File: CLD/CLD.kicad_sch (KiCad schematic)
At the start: 30 parts, among them J1 Conn_01x02, J2 Conn_01x02, J3 Conn_01x02, J4 Conn_01x02, J5 Conn_02x05_Counter_Clockwise, Q1 BSC072N08NS5, U1 STM32F103TBUx, U2 FAN3111E, U3 INA180A1, U4 MCP2551-I-SN

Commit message: update 17/09
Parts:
- removed R2: 50r, symbol Device:R
- removed U1: STM32F103TBUx, Package_DFN_QFN:QFN-36-1EP_6x6mm_P0.5mm_EP4.1x4.1mm, symbol MCU_ST_STM32F1:STM32F103TBUx
- added L1: 0.5uH, Inductor_SMD:L_Bourns-SRN8040_8x8.15mm, symbol Device:L
- added U1: STM32F103CBUx, Package_DFN_QFN:QFN-48-1EP_7x7mm_P0.5mm_EP5.6x5.6mm, symbol MCU_ST_STM32F1:STM32F103CBUx
- C1, C10, C11, C12, C2, C3, C4, C5, C6, C7, C8, C9: footprint (none) -> Capacitor_SMD:C_0201_0603Metric
- D1, D2: footprint (none) -> Diode_SMD:D_0201_0603Metric
- J1, J2, J3, J4: footprint (none) -> Connector_PinHeader_2.54mm:PinHeader_1x02_P2.54mm_Vertical
- J5: footprint (none) -> Connector_PinHeader_1.27mm:PinHeader_2x05_P1.27mm_Vertical_SMD
- R1: footprint (none) -> Resistor_SMD:R_Shunt_Vishay_WSK2512_6332Metric_T1.19mm
- R3, R4, R5, R6: footprint (none) -> Resistor_SMD:R_0201_0603Metric
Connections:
- net +3.3V: now also J5.5 (Pin_5), U1.24 (VDD), U1.36 (VDD), U1.48 (VDD), U1.9 (VDDA)
- net Can_Rx: now also U1.45 (PB8)
- net Can_Tx: now also U1.46 (PB9)
- net Current: now also U1.10 (PA0)
- net GND: now also J5.1 (Pin_1), J5.3 (Pin_3), J5.4 (Pin_4), U1.23 (VSS), U1.35 (VSS), U1.47 (VSS), U1.49 (VSS), U1.8 (VSSA)
- net JTAG_CLK: now also J5.7 (Pin_7), U1.37 (PA14)
- net JTAG_D0: now also J5.8 (Pin_8), U1.39 (PB3)
- net JTAG_D1: now also J5.9 (Pin_9), U1.38 (PA15)
- net JTAG_RST: now also J5.10 (Pin_10), U1.40 (PB4)
- net JTAG_SWDIO: now also J5.6 (Pin_6), U1.34 (PA13)
- net Mos_EN: now also U1.15 (PA5)
- net at Q1.1 (S), Q1.2 (S), Q1.3 (S): now also L1.1
- net at R1.1, U3.3 (+): now also L1.2
- net at D2.1 (K): now also U1.13 (PA3)
- net at D1.1 (K): now also U1.14 (PA4)
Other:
- moved on the sheet: C1, C10, C11, C12, C2, C3, C4, C5, C6, C7, C8, C9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

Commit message: PCB
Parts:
- removed C10, C11, C2, C3, C4: 100n, Capacitor_SMD:C_0201_0603Metric, symbol Device:C
- removed C12, C5: 1u, Capacitor_SMD:C_0201_0603Metric, symbol Device:C
- added C13: 100n, Capacitor_SMD:C_0603_1608Metric, symbol Device:C
- added R2, R7: 10, Resistor_SMD:R_0603_1608Metric, symbol Device:R
- C1, C6, C7, C8, C9: footprint Capacitor_SMD:C_0201_0603Metric -> Capacitor_SMD:C_0603_1608Metric
- D1, D2: footprint Diode_SMD:D_0201_0603Metric -> Diode_SMD:D_0603_1608Metric
- R1: value 0.5mOhm -> 22mOhm; footprint Resistor_SMD:R_Shunt_Vishay_WSK2512_6332Metric_T1.19mm -> Resistor_SMD:R_1206_3216Metric
- R3, R4, R5, R6: footprint Resistor_SMD:R_0201_0603Metric -> Resistor_SMD:R_0603_1608Metric
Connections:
- net GND: now also R7.1; no longer U3.4 (-)
- net at R3.1: now also D1.1 (K); no longer D1.2 (A)
- net at L1.2, R1.1: now also R2.1; no longer U3.3 (+)
- net at D2.1 (K): now also R4.1; no longer U1.13 (PA3)
- net at D2.2 (A): now also U1.13 (PA3); no longer R4.1
- net at U1.14 (PA4): now also D1.2 (A); no longer D1.1 (K)
- new net: C13.1, R2.2, U3.3 (+)
- new net: C13.2, R7.2, U3.4 (-)
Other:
- note removed: "Cap Vin > 25V"
- moved on the sheet: C1, C6, C7, C8, C9, D1, D2, J1, L1, Q1, R1, U2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

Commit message: howdy
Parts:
- added C2, C3: 100n, Capacitor_SMD:C_0603_1608Metric, symbol Device:C
- added D3: LED, Diode_SMD:D_0603_1608Metric, symbol Device:LED
- added R8: 50r, Resistor_SMD:R_0603_1608Metric, symbol Device:R
- added U5: AP2112K-3.3, Package_TO_SOT_SMD:SOT-23-5, symbol Regulator_Linear:AP2112K-3.3
- R3, R4: value R -> 50r
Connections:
- net +3.3V: now also C3.1, U5.5 (VOUT)
- net +5V: now also C2.1, U5.1 (VIN), U5.3 (EN)
- net GND: now also D1.1 (K), D2.1 (K), C2.2, C3.2, D3.1 (K), U5.2 (GND); no longer R3.2, R4.2
- net at R3.1: now also U1.14 (PA4); no longer D1.1 (K)
- net at R4.1: now also U1.13 (PA3); no longer D2.1 (K)
- net at D2.2 (A): now also R4.2; no longer U1.13 (PA3)
- net at D1.2 (A): now also R3.2; no longer U1.14 (PA4)
- net at U1.26 (PB13): now also R8.1
- new net: D3.2 (A), R8.2
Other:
- moved on the sheet: D1, D2

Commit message: PCB routed
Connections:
- net Mos_EN: now also U1.21 (PB10); no longer U1.15 (PA5)
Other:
- company: (none) -> Jack Baker
- title: (none) -> Smart Load Switch
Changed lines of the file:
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@@
 	(generator_version "8.0")
 	(paper "A4")
+	(title_block
+		(title "Smart Load Switch")
+		(date "2024-05-20")
+		(rev "V1.0")
+		(company "Jack Baker")
+	)
 	(junction
 		(at 234.95 31.75)
@@
 		(pts
 			(xy 21.59 31.75) (xy 34.29 31.75)
+		)
+		(stroke
+			(width 0)
+			(type default)
+		)
+	)
+	(wire
+		(pts
+			(xy 24.13 142.24) (xy 33.02 142.24)
 		)
 		(stroke
@@
 		)
 	)
-	(label "Mos_EN"
-		(at 66.04 101.6 0)
-		(fields_autoplaced yes)
-		(effects
-			(font
-				(size 1.27 1.27)
-			)
-			(justify left bottom)
-		)
-	)
 	(label "JTAG_RST"
 		(at 21.59 127 0)
@@
 		(fields_autoplaced yes)
 		(effects
+			(font
+				(size 1.27 1.27)
+			)
+			(justify left bottom)
+		)
+	)
+	(label "Mos_EN"
+		(at 24.13 142.24 0)
+		(fields_autoplaced yes)
+		(effects

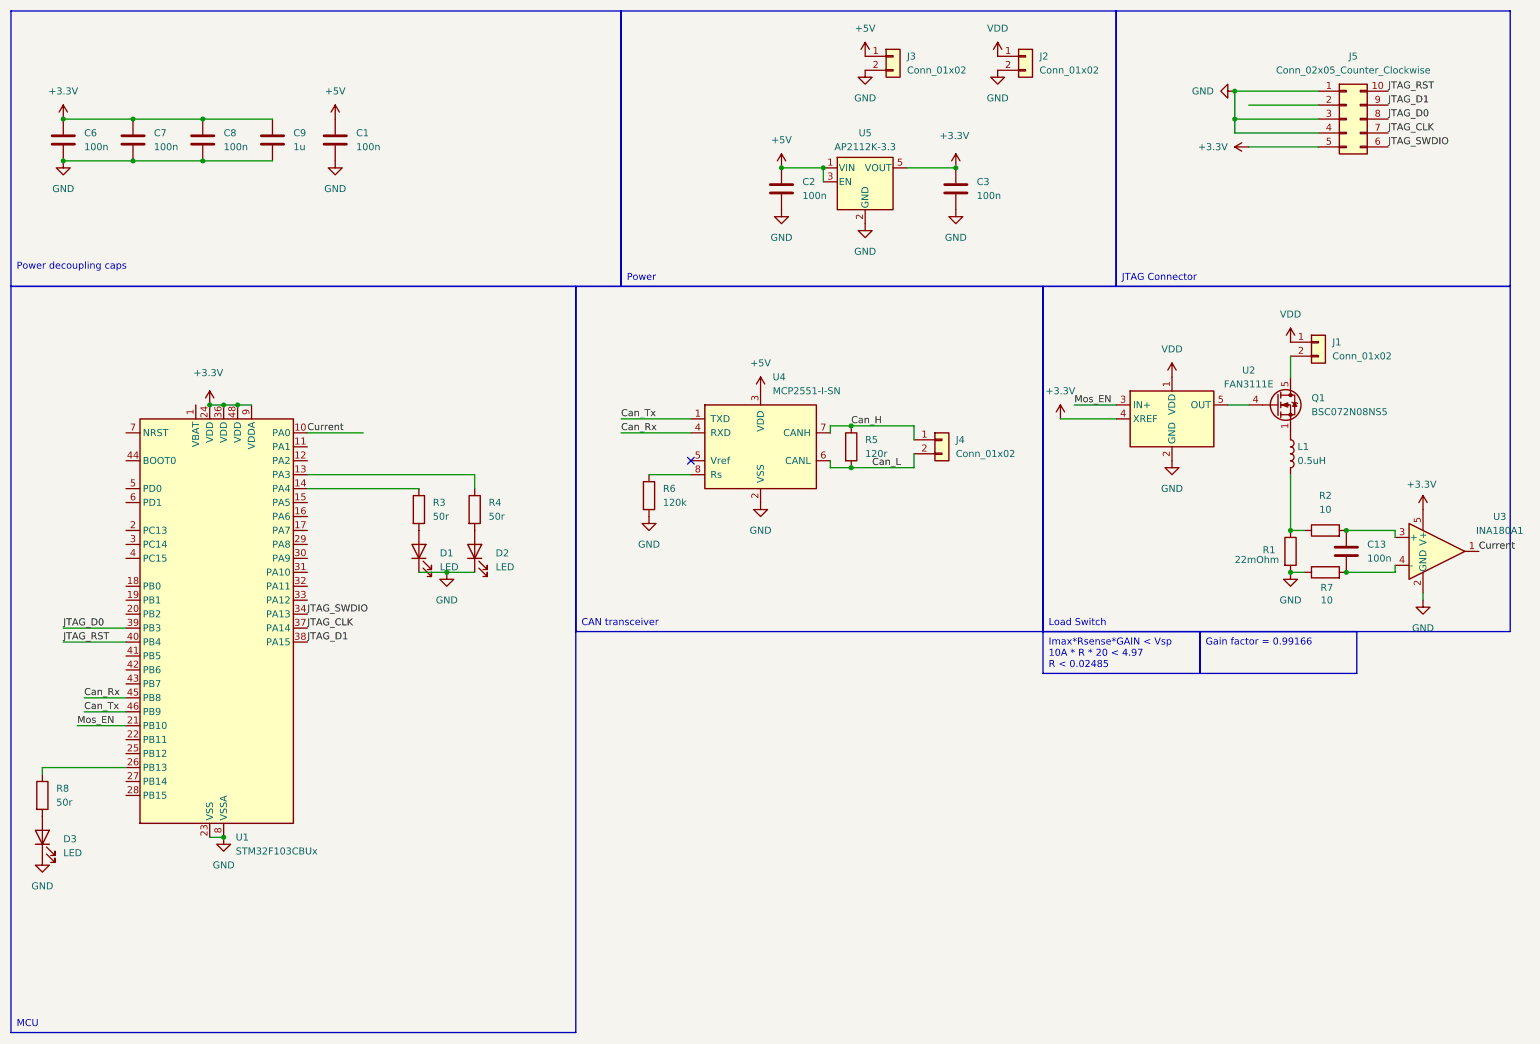
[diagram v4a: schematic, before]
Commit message: add USB + crystal
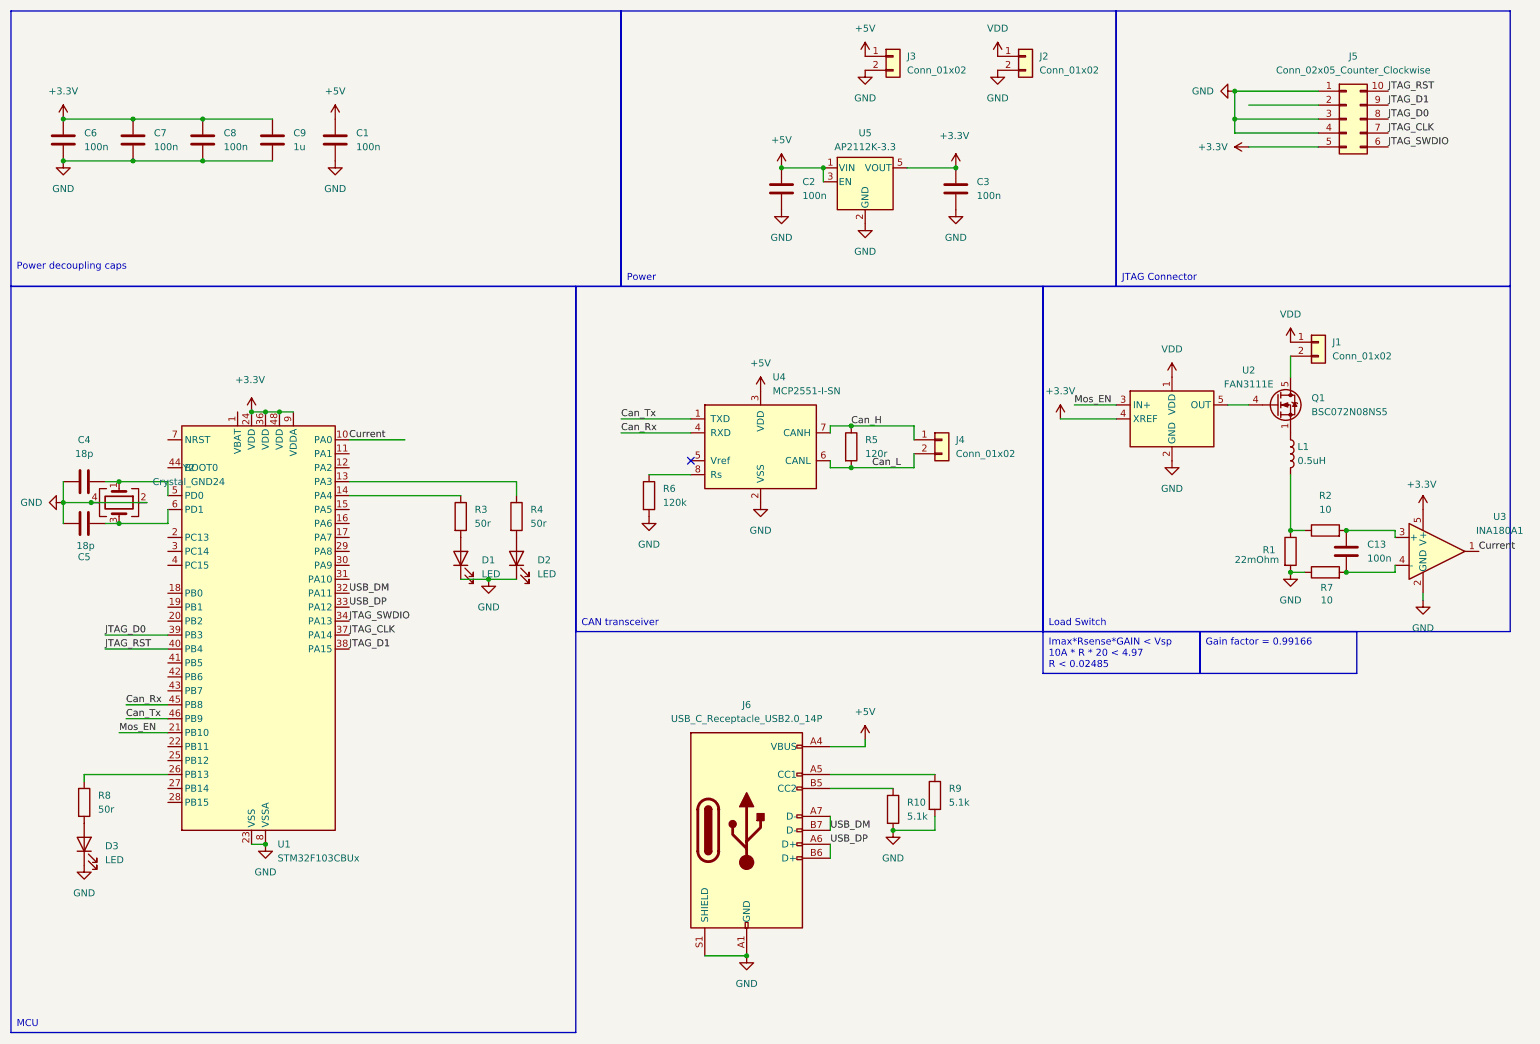
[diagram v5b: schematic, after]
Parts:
- added C4, C5: 18p, Capacitor_SMD:C_0603_1608Metric, symbol Device:C
- added J6: USB_C_Receptacle_USB2.0_14P, Connector_USB:USB_C_Receptacle_GCT_USB4105-xx-A_16P_TopMnt_Horizontal, symbol Connector:USB_C_Receptacle_USB2.0_14P
- added R10, R9: 5.1k, Resistor_SMD:R_0603_1608Metric, symbol Device:R
- added Y2: Crystal_GND24, Crystal:Crystal_SMD_Abracon_ABM3C-4Pin_5.0x3.2mm, symbol Device:Crystal_GND24
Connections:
- net +5V: now also J6.A4 (VBUS), J6.A9 (VBUS), J6.B4 (VBUS), J6.B9 (VBUS)
- net GND: now also C4.1, C5.1, J6.A1 (GND), J6.A12 (GND), J6.B1 (GND), J6.B12 (GND), J6.S1 (SHIELD), R10.2, R9.2, Y2.2, Y2.4
- net USB_DM: now reaches U1.32 (PA11)
- net USB_DM: now also J6.A7 (D-), J6.B7 (D-)
- net USB_DP: now reaches U1.33 (PA12)
- net USB_DP: now also J6.A6 (D+), J6.B6 (D+)
- net at U1.5 (PD0): now also C4.2, Y2.1
- net at U1.6 (PD1): now also C5.2, Y2.3
- new net: J6.A5 (CC1), R9.1
- new net: J6.B5 (CC2), R10.1
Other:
- moved on the sheet: D1, D2, D3, R3, R4, R8, U1

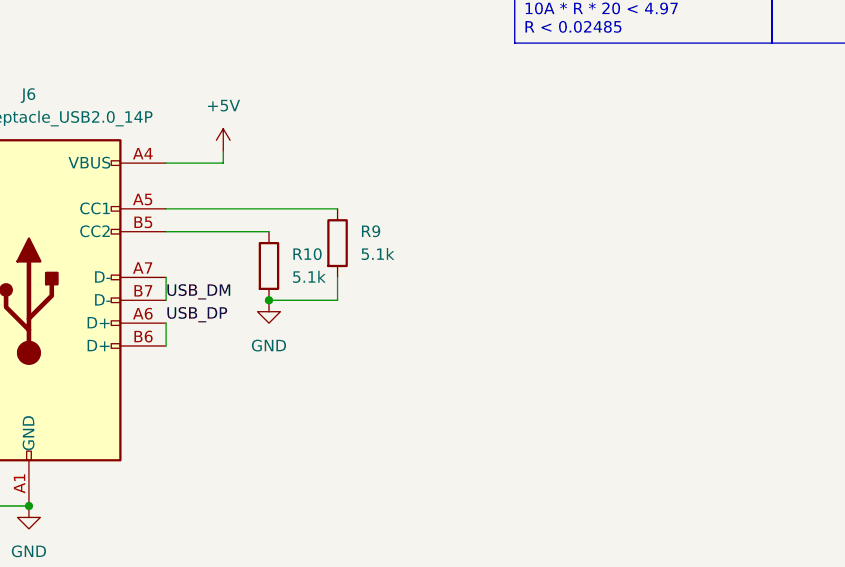
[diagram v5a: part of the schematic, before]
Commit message: added USB serial resistors oops
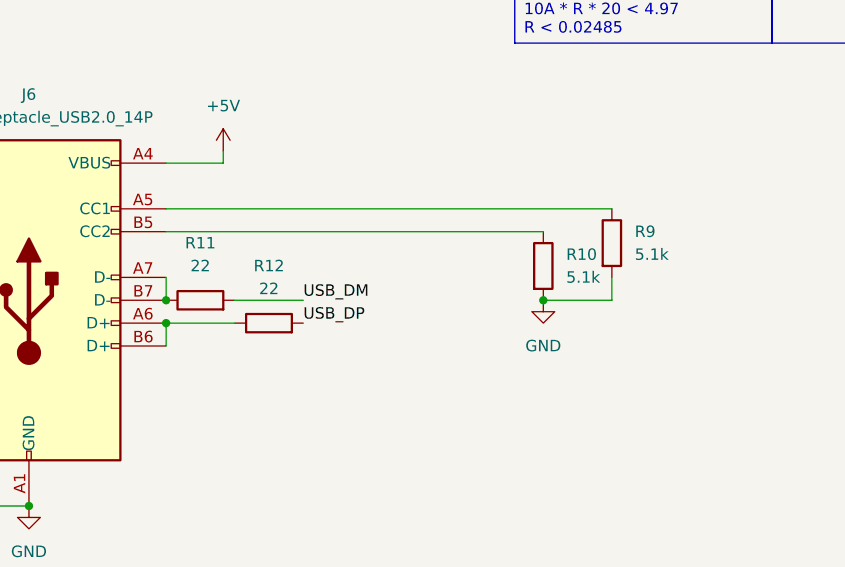
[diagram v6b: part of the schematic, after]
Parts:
- added R11, R12: 22, Resistor_SMD:R_0603_1608Metric, symbol Device:R
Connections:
- net USB_DM: now also R11.2; no longer J6.A7 (D-), J6.B7 (D-)
- net USB_DP: now also R12.2; no longer J6.A6 (D+), J6.B6 (D+)
- new net: J6.A6 (D+), J6.B6 (D+), R12.1
- new net: J6.A7 (D-), J6.B7 (D-), R11.1
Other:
- moved on the sheet: R10, R9
